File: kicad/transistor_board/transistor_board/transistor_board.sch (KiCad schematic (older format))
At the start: 1 part

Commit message: transistor_board
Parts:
- added C1, C2: C, symbol pspice:C
- added C3, C4, C5: C, symbol Device:C
- added D1: D_Bridge_+-AA, symbol Device:D_Bridge_+-AA
- added J1: Conn_01x10, symbol Connector_Generic:Conn_01x10
- added Q1, Q2, Q3: MMBF170, Package_TO_SOT_SMD:SOT-23, symbol Transistor_FET:MMBF170
- added R1, R2: R, symbol Device:R
- added U1: DRV8872DDAR, DDA0008H_N_TEX, symbol 2020-07-29_12-21-43:DRV8872DDAR
- added U3: LM7805_TO220, Package_TO_SOT_THT:TO-220-3_Vertical, symbol Regulator_Linear:LM7805_TO220
- gave numbers to parts that had none: 1
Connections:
- net at U2.1 (5V): now also C4.1
- net at U2.15 (IO16): now also U1.4 (FAULT_N)
- net at U2.16 (3V3): now also C5.1, U3.3 (VO)
- net GND: now reaches U2.2 (GND)
- net GND: now also C1.2, C2.2, C3.2, C4.2, C5.2, D1.2 (-), J1.1 (Pin_1), Q1.2 (S), Q2.2 (S), Q3.2 (S), R2.2, U1.1 (GND), U1.9 (PAD), U3.2 (GND)
- net at U2.3 (IO12): now also U1.3 (IN1)
- net at U2.4 (IO4): now also U1.2 (IN2)
- net at U2.5 (IO15): now also Q2.1 (G)
- net at U2.6 (IO14): now also Q1.1 (G)
- net at U2.7 (IO2): now also Q3.1 (G)
- new net: C3.1, D1.1 (+), R1.1
- new net: D1.3 (~~), J1.10 (Pin_10)
- new net: D1.4 (~~), J1.9 (Pin_9)
- new net: J1.2 (Pin_2), J1.3 (Pin_3), R1.2, U3.1 (VI)
- new net: J1.4 (Pin_4), U1.6 (OUT1)
- new net: J1.5 (Pin_5), U1.8 (OUT2)
- new net: J1.6 (Pin_6), Q3.3 (D)
- new net: J1.7 (Pin_7), Q2.3 (D)
- new net: J1.8 (Pin_8), Q1.3 (D)
- new net: C1.1, C2.1, U1.5 (VM)
- new net: R2.1, U1.7 (ISEN)
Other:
- moved on the sheet: U2

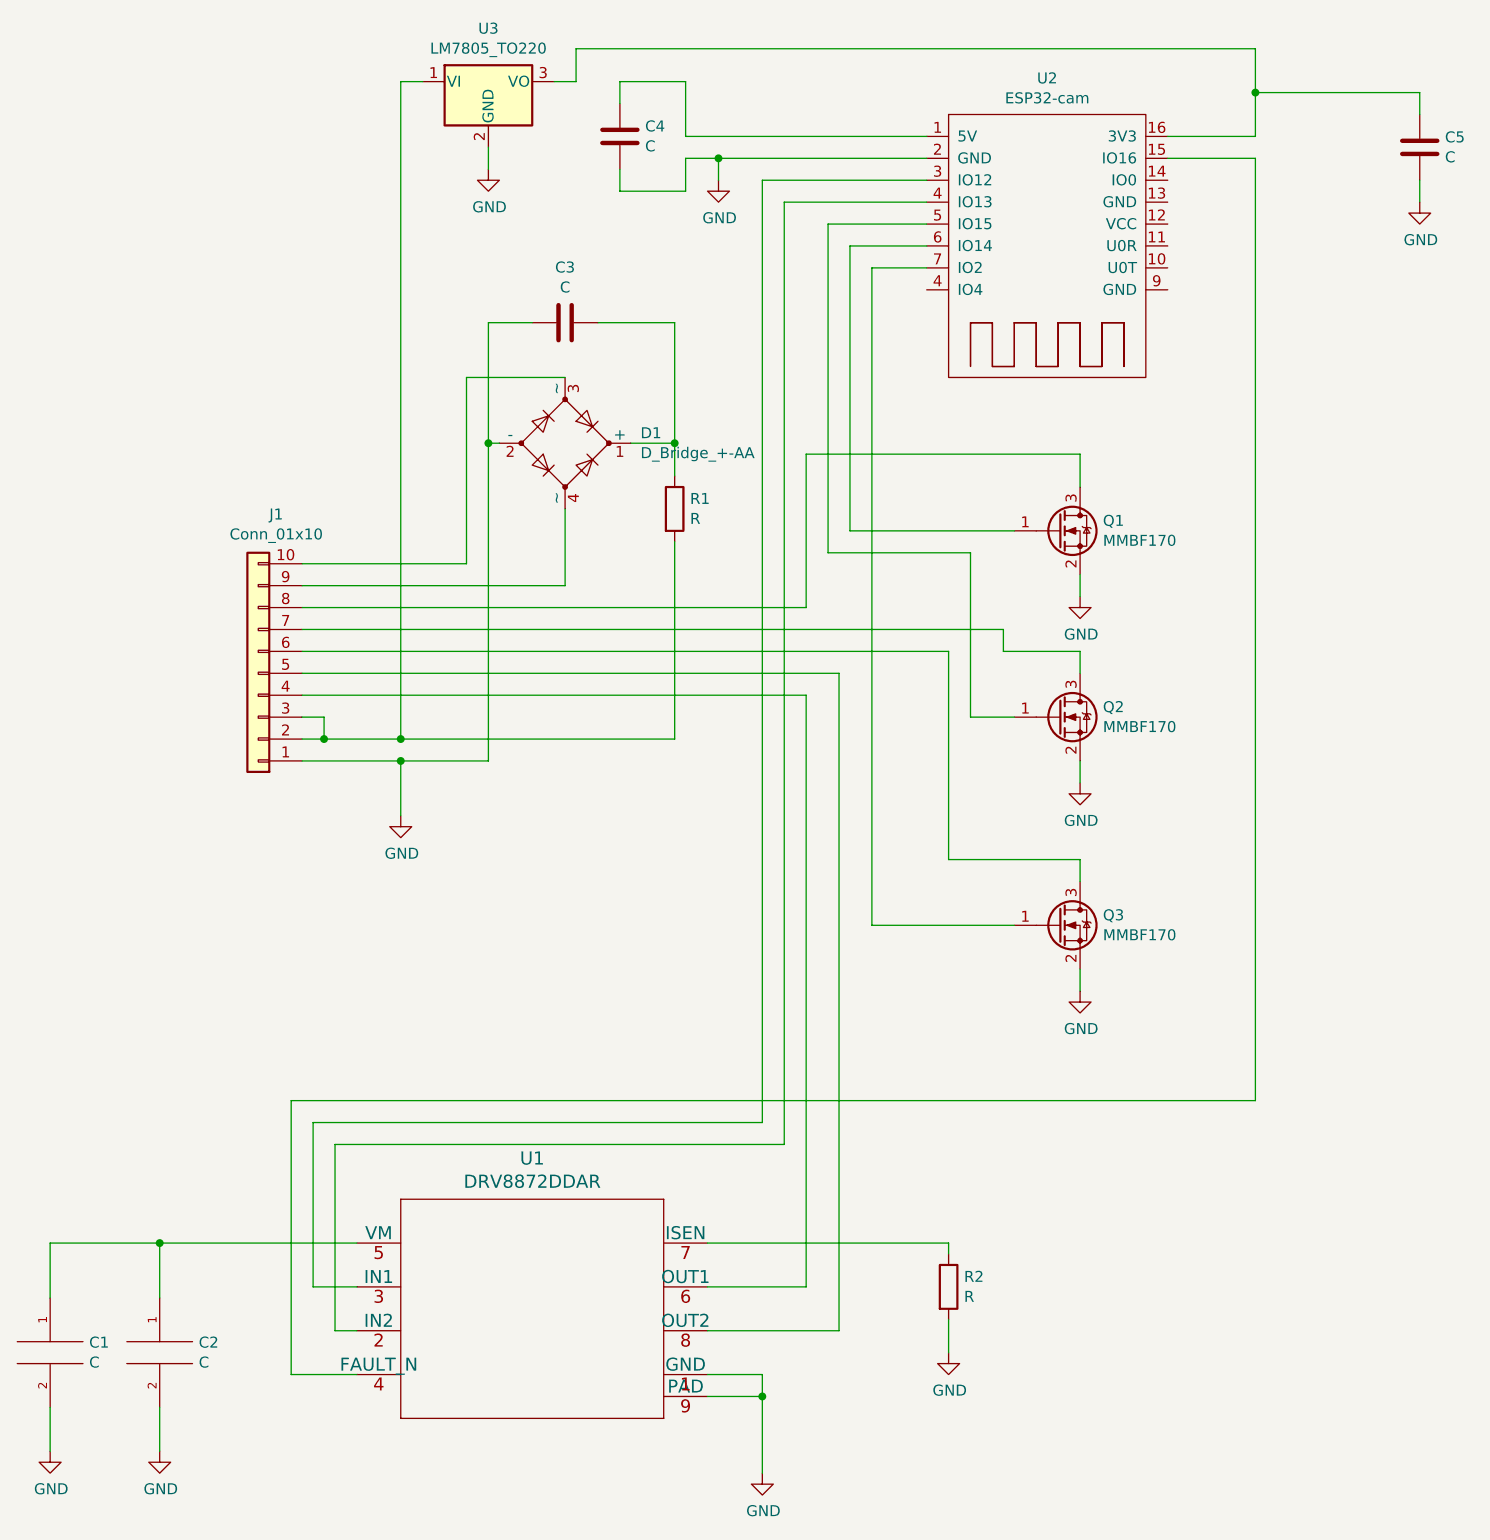
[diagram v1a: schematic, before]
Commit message: motor not powered via resistor
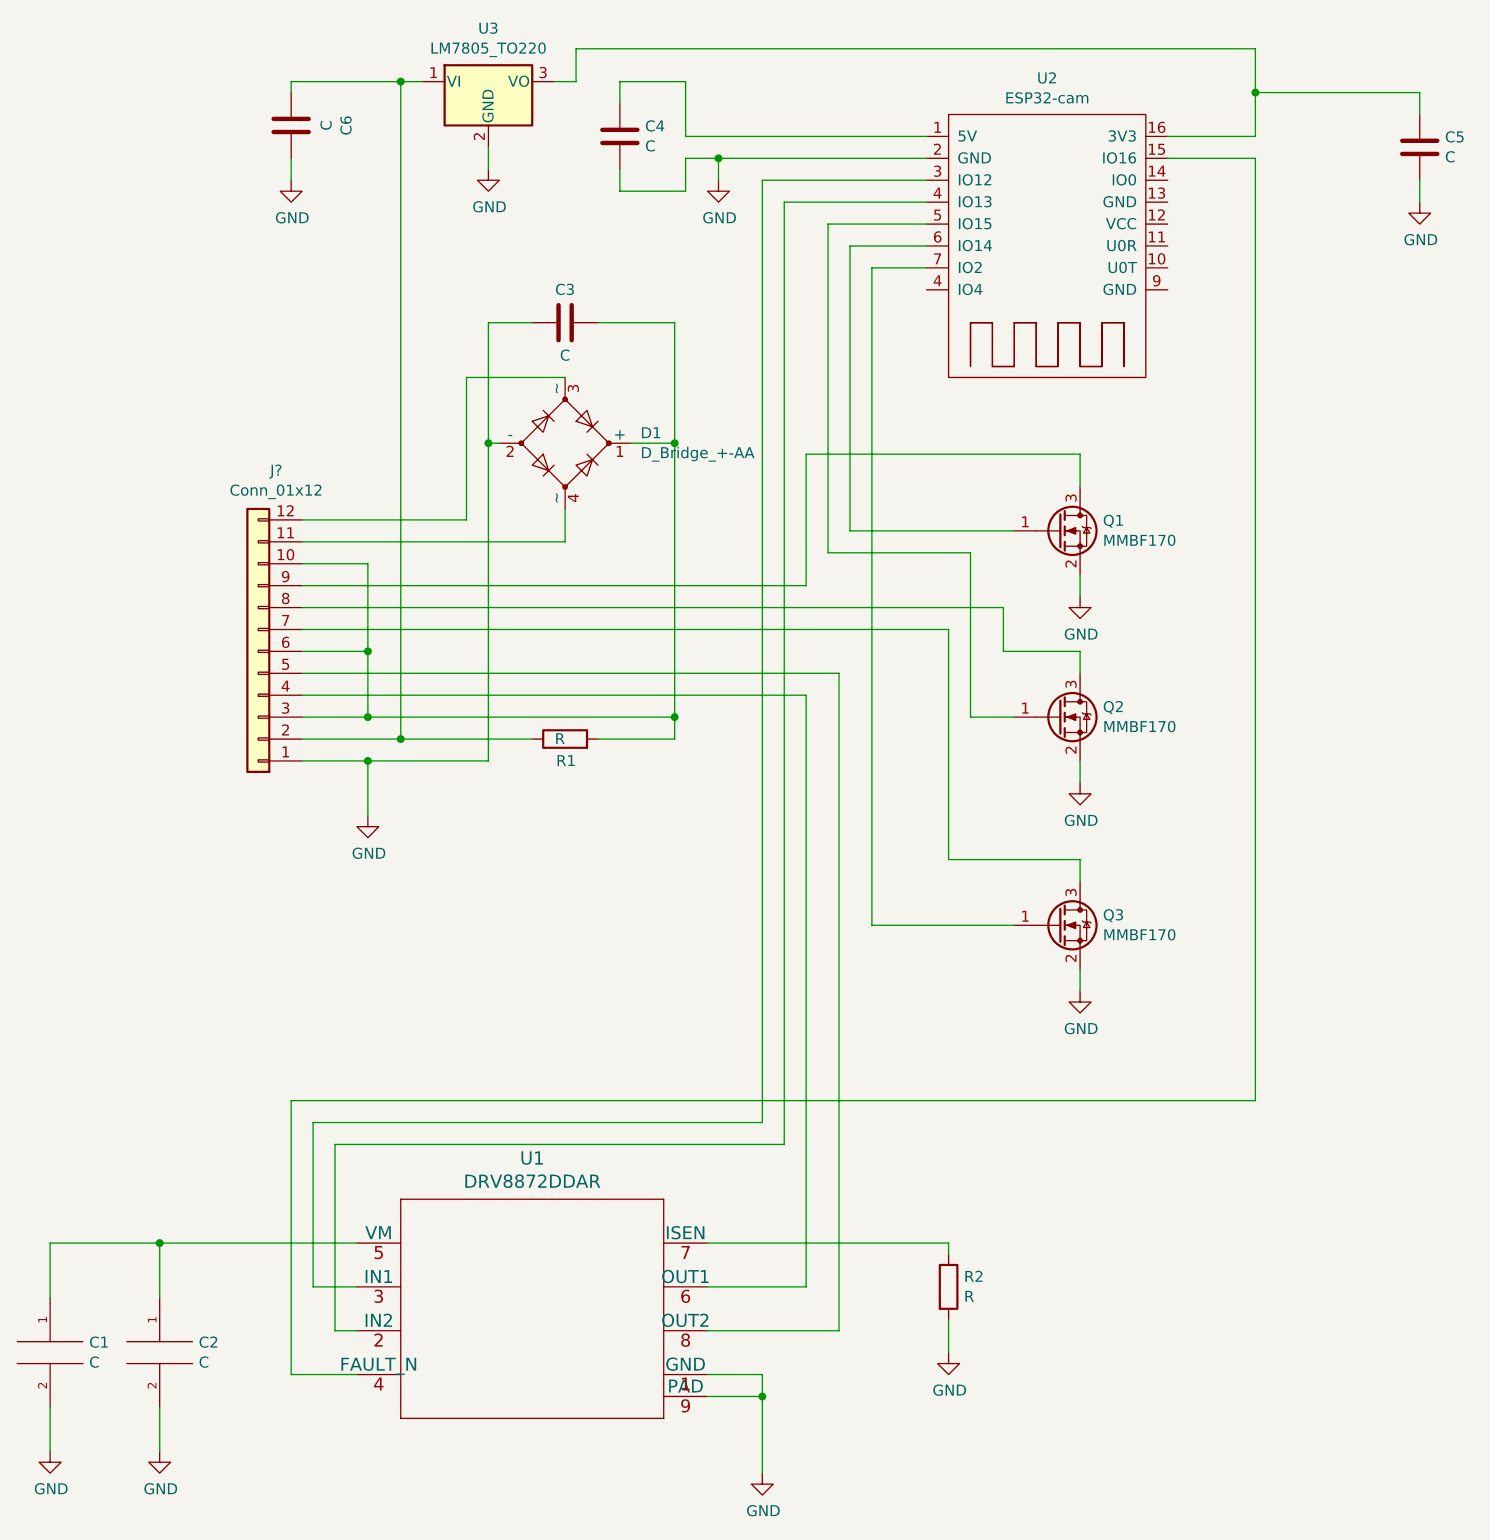
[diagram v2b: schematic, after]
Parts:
- removed J1: Conn_01x10, symbol Connector_Generic:Conn_01x10
- added C6: C, symbol Device:C
- added J?: Conn_01x12, symbol Connector_Generic:Conn_01x12
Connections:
- net GND: now also C6.1, J?.1 (Pin_1)
- net at U2.4 (IO4): now also U1.2 (IN2)
- net at C3.1, D1.1 (+): now also R1.2, J?.10 (Pin_10), J?.3 (Pin_3), J?.6 (Pin_6); no longer R1.1
- net at D1.3 (~~): now also J?.12 (Pin_12)
- net at D1.4 (~~): now also J?.11 (Pin_11)
- net at U3.1 (VI): now also R1.1, C6.2, J?.2 (Pin_2); no longer R1.2
- net at U1.6 (OUT1): now also J?.4 (Pin_4)
- net at U1.8 (OUT2): now also J?.5 (Pin_5)
- net at Q3.3 (D): now also J?.7 (Pin_7)
- net at Q2.3 (D): now also J?.8 (Pin_8)
- net at Q1.3 (D): now also J?.9 (Pin_9)
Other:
- moved on the sheet: R1
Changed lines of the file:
@@
 	1    0    0    -1
 $EndComp
-$Comp
-L Connector_Generic:Conn_01x10 J1
-U 1 1 5F21AB9A
-P 3500 3550
-F 0 "J1" H 3418 2825 50  0000 C CNN
-F 1 "Conn_01x10" H 3418 2916 50  0000 C CNN
-F 2 "" H 3500 3550 50  0001 C CNN
-F 3 "~" H 3500 3550 50  0001 C CNN
-	1    3500 3550
-	-1   0    0    1
-$EndComp
-Wire Wire Line
-	3700 3050 4450 3050
-Wire Wire Line
-	4450 3050 4450 2200
 Wire Wire Line
 	4450 2200 4900 2200
 Wire Wire Line
-	4900 2800 4900 3150
-Wire Wire Line
-	4900 3150 3700 3150
+	4900 2800 4900 2950
 Wire Wire Line
 	4600 2500 4550 2500
@@
 	4550 2500 4550 3950
 Wire Wire Line
-	4550 3950 4150 3950
+	4550 3950 4000 3950
 $Comp
 L power:GND #PWR03
 U 1 1 5F21C64D
-P 4150 4200
-F 0 "#PWR03" H 4150 3950 50  0001 C CNN
-F 1 "GND" H 4155 4027 50  0000 C CNN
-F 2 "" H 4150 4200 50  0001 C CNN
-F 3 "" H 4150 4200 50  0001 C CNN
-	1    4150 4200
-	1    0    0    -1
-$EndComp
-Wire Wire Line
-	4150 4200 4150 3950
-Connection ~ 4150 3950
-Wire Wire Line
-	4150 3950 3700 3950
-Wire Wire Line
-	3700 3850 3800 3850
+P 4000 4200
+F 0 "#PWR03" H 4000 3950 50  0001 C CNN
+F 1 "GND" H 4005 4027 50  0000 C CNN
+F 2 "" H 4000 4200 50  0001 C CNN
+F 3 "" H 4000 4200 50  0001 C CNN
+	1    4000 4200
+	1    0    0    -1
+$EndComp
+Wire Wire Line
+	4000 4200 4000 3950
+Connection ~ 4000 3950
+Wire Wire Line
+	4000 3950 3700 3950
 Wire Wire Line
 	5200 2500 5400 2500
@@
 L Device:R R1
 U 1 1 5F21E564
-P 5400 2800
-F 0 "R1" H 5470 2846 50  0000 L CNN
-F 1 "R" H 5470 2755 50  0000 L CNN
-F 2 "" V 5330 2800 50  0001 C CNN
-F 3 "~" H 5400 2800 50  0001 C CNN
-	1    5400 2800
-	1    0    0    -1
-$EndComp
-Wire Wire Line
-	5400 2500 5400 2650
-Wire Wire Line
-	5400 2950 5400 3850
+P 4900 3850
+F 0 "R1" V 4800 3800 50  0000 L CNN
+F 1 "R" V 4900 3850 50  0000 L CNN
+F 2 "" V 4830 3850 50  0001 C CNN
+F 3 "~" H 4900 3850 50  0001 C CNN
+	1    4900 3850
+	0    -1   -1   0
+$EndComp
 $Comp
 L 2020-07-29_12-21-43:DRV8872DDAR U1
@@
 	5800 6850 5800 6750
 Wire Wire Line
-	3800 3850 3800 3750
-Wire Wire Line
-	3800 3750 3700 3750
-Connection ~ 3800 3850
-Wire Wire Line
-	3800 3850 4150 3850
-Wire Wire Line
 	5550 6350 6000 6350
 Wire Wire Line
@@
 	7250 2550 6000 2550
 Wire Wire Line
-	6000 2550 6000 3250
-Wire Wire Line
-	6000 3250 3700 3250
+	6000 2550 6000 3150
 Wire Wire Line
 	7250 3550 7250 3450
 Wire Wire Line
 	7250 3450 6900 3450
-Wire Wire Line
-	6900 3450 6900 3350
-Wire Wire Line
-	6900 3350 3700 3350
 $Comp
 L Transistor_FET:MMBF170 Q3
@@
 Wire Wire Line
 	7250 4400 6650 4400
-Wire Wire Line
-	6650 4400 6650 3450
-Wire Wire Line
-	6650 3450 3700 3450
 Connection ~ 4550 2500
 Connection ~ 5400 2500
@@
 U 1 1 5F313280
 P 4900 1950
-F 0 "C3" V 4648 1950 50  0000 C CNN
-F 1 "C" V 4739 1950 50  0000 C CNN
+F 0 "C3" V 4750 1950 50  0000 C CNN
+F 1 "C" V 5050 1950 50  0000 C CNN
 F 2 "" H 4938 1800 50  0001 C CNN
 F 3 "~" H 4900 1950 50  0001 C CNN
@@
 Wire Wire Line
 	4150 850  4250 850
+Wire Wire Line
+	4150 850  4150 3850
+$Comp
+L Device:C C6
+U 1 1 5F24F95F
+P 3650 1050
+F 0 "C6" V 3398 1050 50  0000 C CNN
+F 1 "C" V 3489 1050 50  0000 C CNN
+F 2 "" H 3688 900 50  0001 C CNN
+F 3 "~" H 3650 1050 50  0001 C CNN
+	1    3650 1050
+	-1   0    0    1
+$EndComp
+Wire Wire Line
+	3650 900  3650 850
+Wire Wire Line
+	3650 850  4150 850
+Connection ~ 4150 850
+$Comp
+L power:GND #PWR012
+U 1 1 5F253D6E
+P 3650 1300
+F 0 "#PWR012" H 3650 1050 50  0001 C CNN
+F 1 "GND" H 3655 1127 50  0000 C CNN
+F 2 "" H 3650 1300 50  0001 C CNN
+F 3 "" H 3650 1300 50  0001 C CNN
+	1    3650 1300
+	1    0    0    -1
+$EndComp
+Wire Wire Line
+	3650 1300 3650 1200
+Wire Wire Line
+	5050 3850 5400 3850
+Wire Wire Line
+	5400 2500 5400 3750
+Wire Wire Line
+	3700 3850 4150 3850
 Connection ~ 4150 3850
 Wire Wire Line
-	4150 3850 5400 3850
-Wire Wire Line
-	4150 850  4150 3850
+	4150 3850 4750 3850
+Wire Wire Line
+	5400 3750 4000 3750
+Connection ~ 5400 3750
+Wire Wire Line
+	5400 3750 5400 3850
+$Comp
+L Connector_Generic:Conn_01x12 J?
+U 1 1 5F29655C
+P 3500 3450
+F 0 "J?" H 3418 2625 50  0000 C CNN
+F 1 "Conn_01x12" H 3418 2716 50  0000 C CNN
+F 2 "" H 3500 3450 50  0001 C CNN
+F 3 "~" H 3500 3450 50  0001 C CNN
+	1    3500 3450
+	-1   0    0    1
+$EndComp
+Wire Wire Line
+	3700 2850 4450 2850
+Wire Wire Line
+	4450 2200 4450 2850
+Wire Wire Line
+	3700 2950 4900 2950
+Wire Wire Line
+	6000 3150 3700 3150
+Wire Wire Line
+	4000 3050 3700 3050
+Wire Wire Line
+	3700 3250 6900 3250
+Wire Wire Line
+	6900 3250 6900 3450
+Wire Wire Line
+	3700 3350 6650 3350
+Wire Wire Line
+	6650 3350 6650 4400
+Wire Wire Line
+	3700 3450 4000 3450
+Wire Wire Line
+	4000 3450 4000 3750
+Connection ~ 4000 3750
+Wire Wire Line
+	4000 3750 3700 3750
+Wire Wire Line
+	4000 3450 4000 3050
+Connection ~ 4000 3450
 $EndSCHEMATC
